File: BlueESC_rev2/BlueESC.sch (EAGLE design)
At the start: 76 parts, among them Q1 BC817-40W, Q2 BC817-40W, Q3 BC817-40W, Q4 SI7370, Q5 SI7370, Q6 SI7370, Q7 SI7370, Q8 SI7370, Q9 SI7370, U1 ATMEGA168MLF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

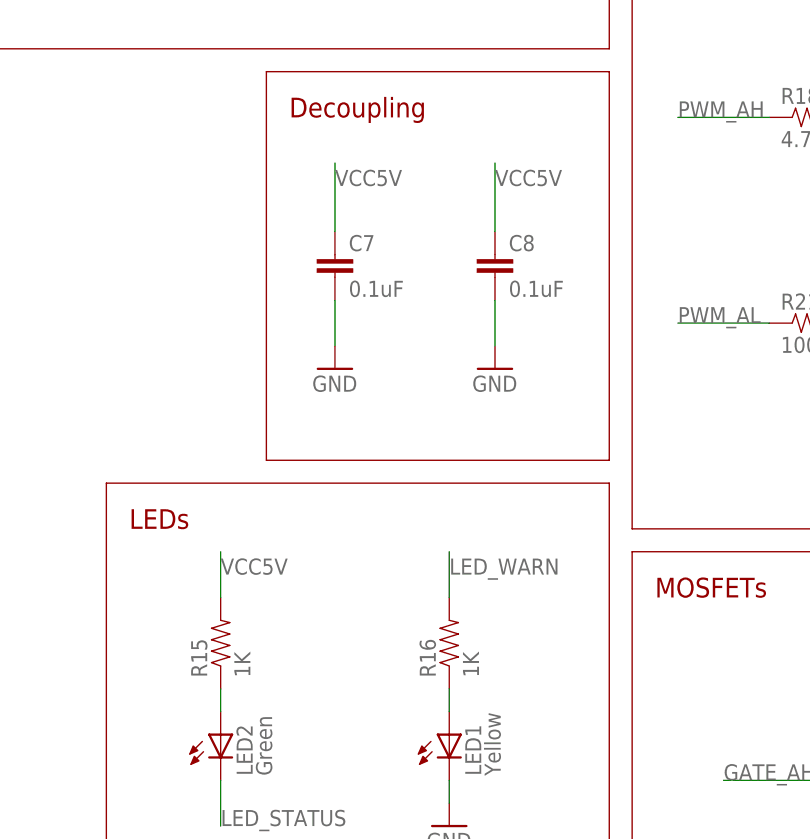
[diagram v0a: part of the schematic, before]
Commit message: Placed more components on board layout.
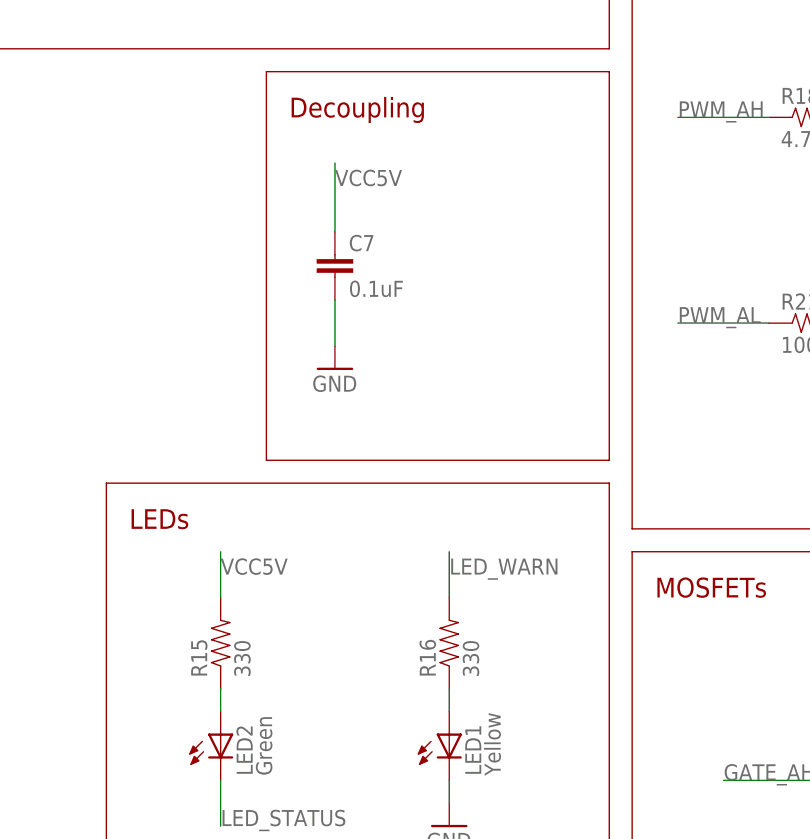
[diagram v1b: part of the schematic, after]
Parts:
- removed C8: 0.1uF, SparkFun-Capacitors:CAP0603-CAP
- R15, R16: value 1K -> 330
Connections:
- net GND: no longer C8.2
- net VCC5V: no longer C8.1
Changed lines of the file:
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@@
 <part name="GND9" library="SparkFun" deviceset="GND" device=""/>
 <part name="Y1" library="SparkFun" deviceset="RESONATOR" device="SMD"/>
-<part name="R15" library="SparkFun" deviceset="RESISTOR" device="0603-RES" value="1K"/>
+<part name="R15" library="SparkFun" deviceset="RESISTOR" device="0603-RES" value="330"/>
 <part name="LED2" library="SparkFun" deviceset="LED" device="-3MM-NO_SILK" value="Green"/>
-<part name="R16" library="SparkFun" deviceset="RESISTOR" device="0603-RES" value="1K"/>
+<part name="R16" library="SparkFun" deviceset="RESISTOR" device="0603-RES" value="330"/>
 <part name="LED1" library="SparkFun" deviceset="LED" device="-3MM-NO_SILK" value="Yellow"/>
 <part name="GND7" library="SparkFun" deviceset="GND" device=""/>
 <part name="C7" library="SparkFun-Capacitors" deviceset="CAP" device="0603-CAP" value="0.1uF"/>
-<part name="C8" library="SparkFun-Capacitors" deviceset="CAP" device="0603-CAP" value="0.1uF"/>
 <part name="GND8" library="SparkFun-Aesthetics" deviceset="GND" device=""/>
-<part name="GND10" library="SparkFun-Aesthetics" deviceset="GND" device=""/>
 <part name="R17" library="SparkFun-Resistors" deviceset="33KOHM1/10W1%(0603)" device="" value="2.2K"/>
 <part name="R18" library="SparkFun-Resistors" deviceset="33KOHM1/10W1%(0603)" device="" value="4.7K"/>
@@
 <instance part="GND7" gate="1" x="187.96" y="2.54"/>
 <instance part="C7" gate="G$1" x="175.26" y="63.5"/>
-<instance part="C8" gate="G$1" x="193.04" y="63.5"/>
 <instance part="GND8" gate="1" x="175.26" y="53.34"/>
-<instance part="GND10" gate="1" x="193.04" y="53.34"/>
 <instance part="R17" gate="G$1" x="246.38" y="96.52" rot="R90"/>
 <instance part="R18" gate="G$1" x="228.6" y="81.28"/>
@@
 </segment>
 <segment>
-<pinref part="C8" gate="G$1" pin="2"/>
-<pinref part="GND10" gate="1" pin="GND"/>
-<wire x1="193.04" y1="60.96" x2="193.04" y2="55.88" width="0.1524" layer="91"/>
-</segment>
-<segment>
 <pinref part="GND11" gate="1" pin="GND"/>
 <pinref part="Q1" gate="G$1" pin="E"/>
@@
 </segment>
 <segment>
-<pinref part="C8" gate="G$1" pin="1"/>
-<wire x1="193.04" y1="68.58" x2="193.04" y2="76.2" width="0.1524" layer="91"/>
-<label x="193.04" y="73.66" size="1.778" layer="95"/>
-</segment>
-<segment>

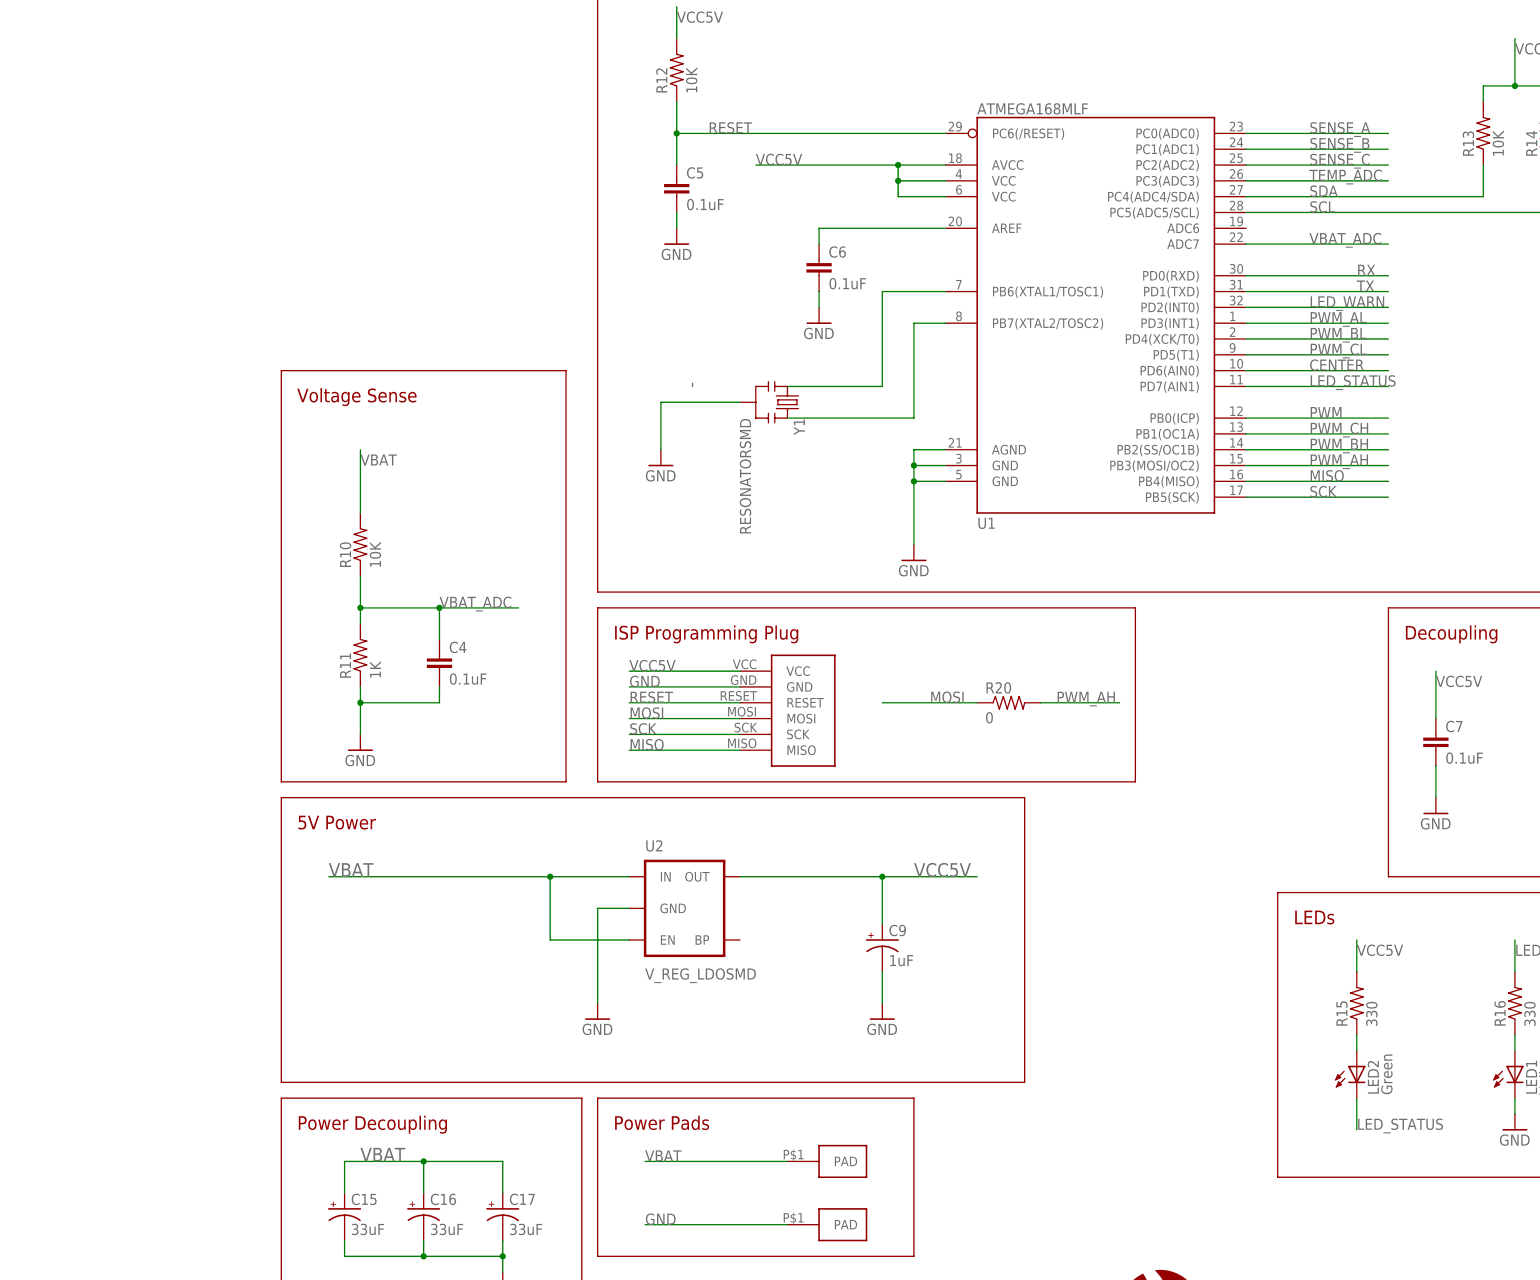
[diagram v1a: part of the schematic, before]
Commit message: Added ACS71X to the schematic and board layout to measure current.
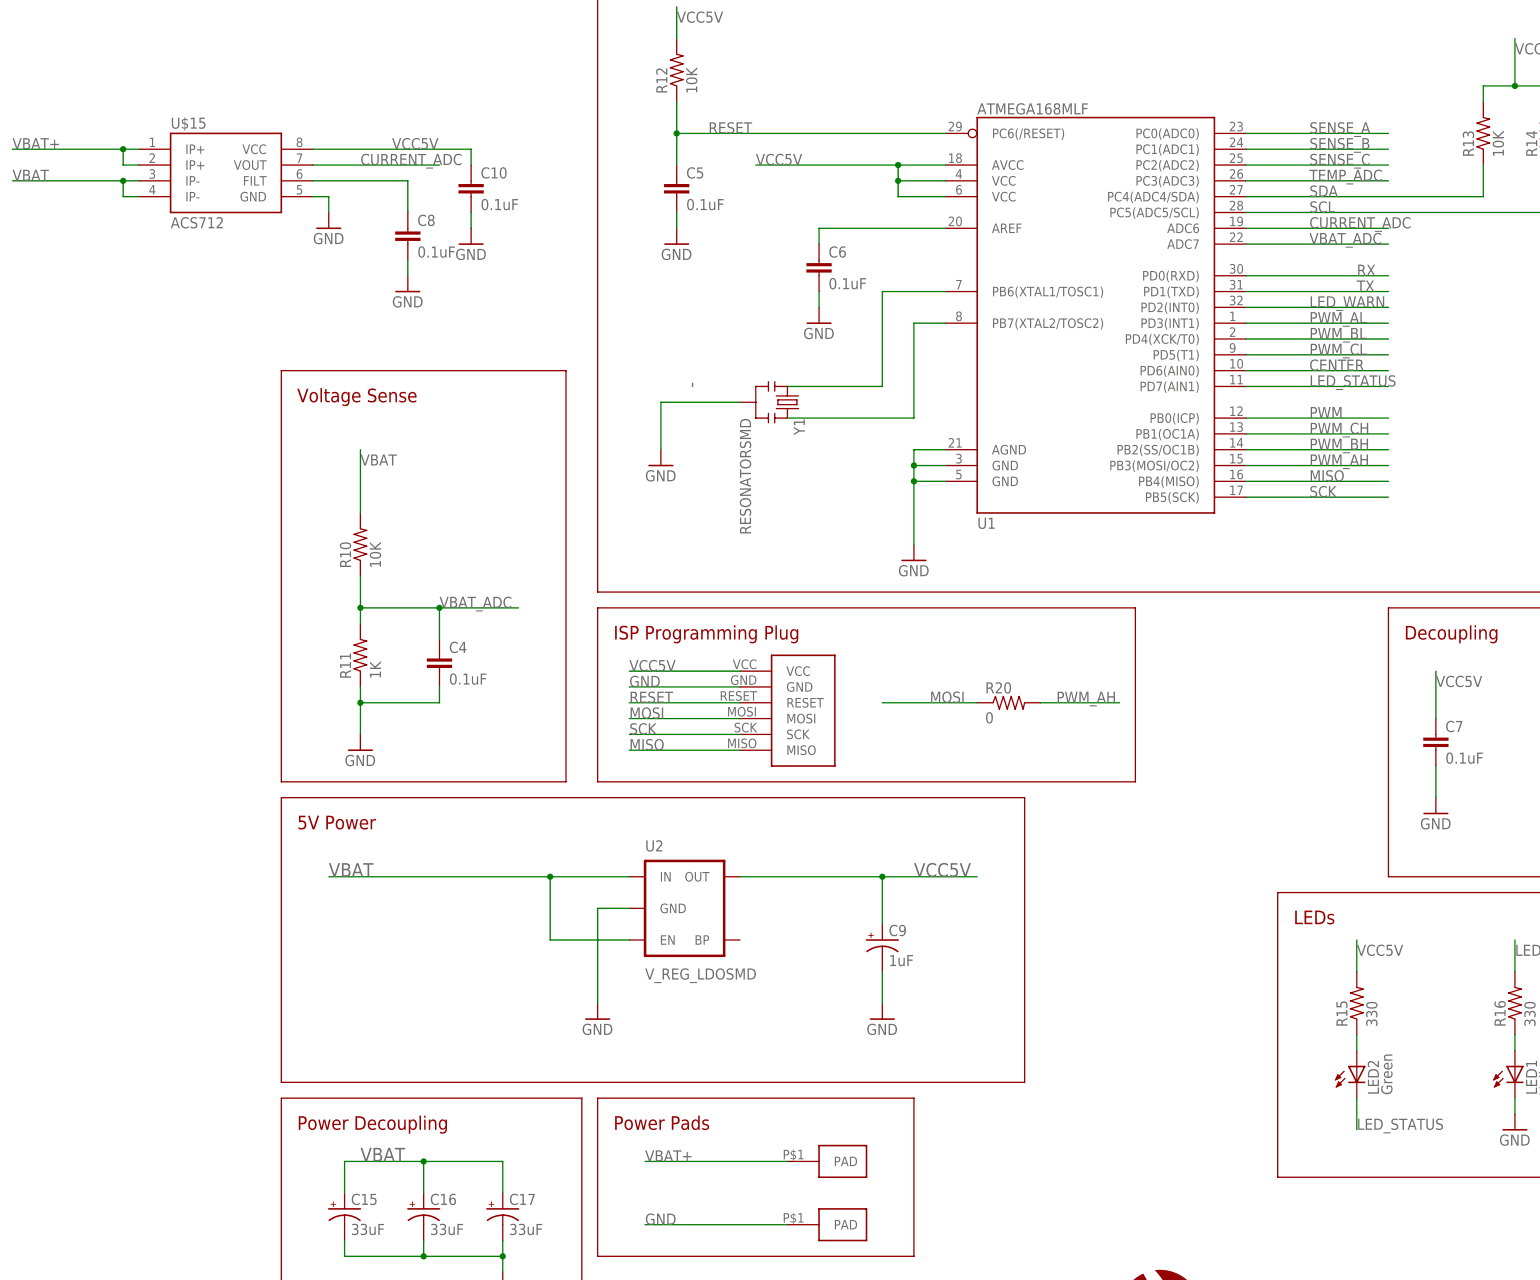
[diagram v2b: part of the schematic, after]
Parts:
- added C10, C8: 0.1uF, SparkFun-Capacitors:CAP0603-CAP
- added U$15: ACS712, SparkFun-AnalogIC:ACS712
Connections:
- new net CURRENT_ADC: U$15.VOUT, U1.ADC6
- new net N$1: C8.1, U$15.FILT
- new net VBAT+: U$1.PAD, U$15.IP+@1, U$15.IP+@2
- net GND: now also C10.2, C8.2, U$15.GND
- net VBAT: now also U$15.IP-@3, U$15.IP-@4; no longer U$1.PAD
- net VCC5V: now also C10.1, U$15.VCC
